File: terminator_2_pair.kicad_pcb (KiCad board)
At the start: 2 copper layers, 70.5 x 41.9 mm, 1 part

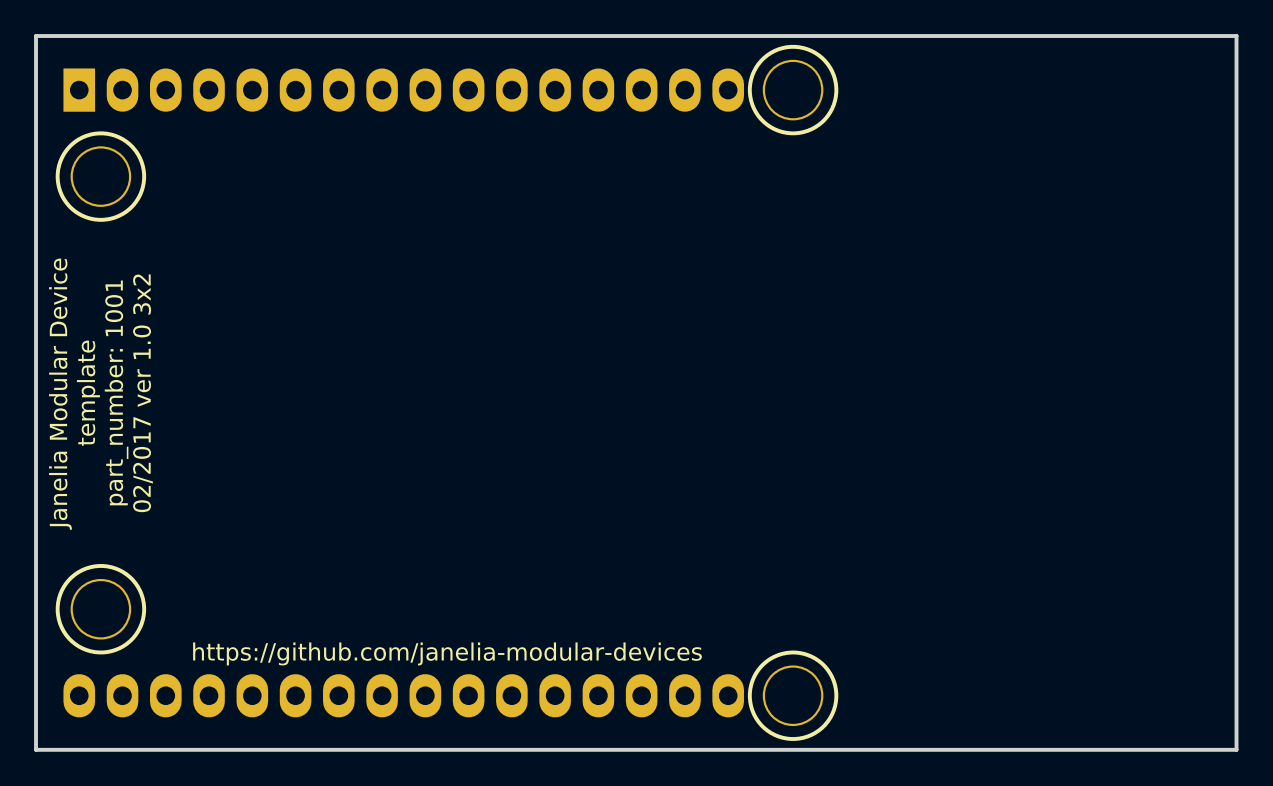
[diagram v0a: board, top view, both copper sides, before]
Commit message: Added footprints and components.
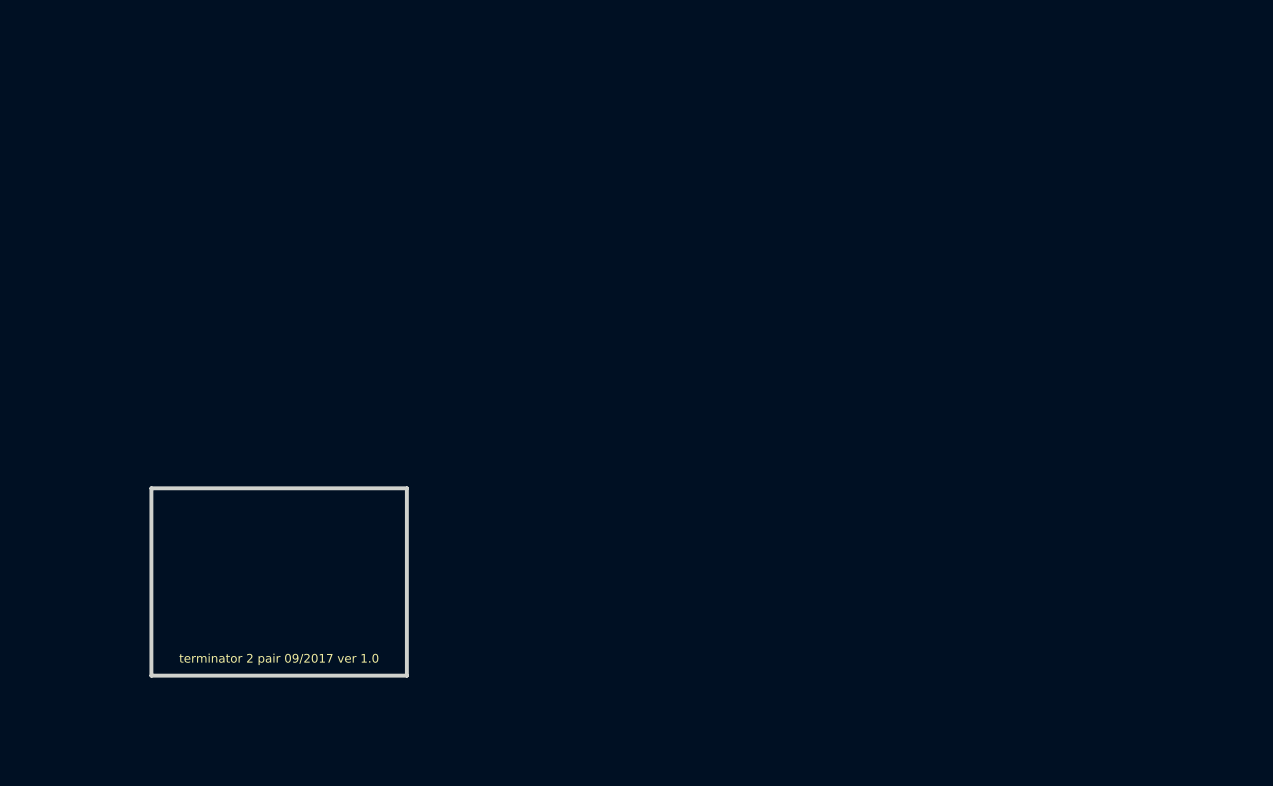
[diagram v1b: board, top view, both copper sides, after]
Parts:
- removed MDB1: MODULAR_DEVICE_BASE_3X2_MALE, terminator_2_pair:MODULAR_DEVICE_BASE_3X2_MALE
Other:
- board size 70.5 x 41.9 mm -> 15 x 11 mm
- net class Default: trace_width 0.254 -> 0.25
- board text added: "terminator 2 pair 09/2017 ver 1.0"
- board text removed: "Janelia Modular Device template part_number: 1001 02/2017 ver 1.0 3x2"
- board text removed: "https://github.com/janelia-modular-devices"
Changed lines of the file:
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@@
-(kicad_pcb (version 20170123) (host pcbnew no-vcs-found-0633d90~59~ubuntu16.04.1)
+(kicad_pcb (version 20170123) (host pcbnew no-vcs-found-33cc7b3~60~ubuntu16.04.1)
   (general
     (thickness 1.6)
-    (drawings 6)
+    (drawings 5)
     (tracks 0)
     (zones 0)
-    (modules 1)
+    (modules 0)
     (nets 1)
   )
@@
   )
   (setup
-    (last_trace_width 0.254)
+    (last_trace_width 0.25)
     (trace_clearance 0.0254)
     (zone_clearance 0.2032)
@@
       (layerselection 0x000f0_ffffffff)
       (usegerberextensions true)
+      (usegerberattributes true)
+      (usegerberadvancedattributes true)
+      (creategerberjobfile true)
       (excludeedgelayer false)
       (linewidth 0.100000)
@@
   (net_class Default "This is the default net class."
     (clearance 0.0254)
-    (trace_width 0.254)
+    (trace_width 0.25)
     (via_dia 0.889)
     (via_drill 0.635)
     (uvia_dia 0.508)
     (uvia_drill 0.127)
-    (diff_pair_gap 0.254)
-    (diff_pair_width 0.254)
   )
   (net_class GND ""
@@
     (diff_pair_width 0.254)
   )
-  (module terminator_2_pair:MODULAR_DEVICE_BASE_3X2_MALE (layer F.Cu)
-    (at 107.315 88.9)
-    (fp_text reference MDB1 (at 0 0) (layer F.SilkS) hide
-      (effects (font (size 1.016 1.016) (thickness 0.254)))
-    )
-    (fp_text value MODULAR_DEVICE_BASE_3X2_MALE (at 0 2.54) (layer F.SilkS) hide
-      (effects (font (thickness 0.3048)))
-    )
-    (fp_line (start 48.895 -20.955) (end -21.59 -20.955) (layer F.Fab) (width 0.2286))
-    (fp_line (start 48.895 20.955) (end 48.895 -20.955) (layer F.Fab) (width 0.2286))
-    (fp_line (start -21.59 20.955) (end 48.895 20.955) (layer F.Fab) (width 0.2286))
-    (fp_line (start -21.59 -20.955) (end -21.59 20.955) (layer F.Fab) (width 0.2286))
-    (fp_line (start 20.32 -19.05) (end -20.32 -19.05) (layer B.SilkS) (width 0.381))
-    (fp_line (start 20.32 -16.51) (end 20.32 -19.05) (layer B.SilkS) (width 0.381))
-    (fp_line (start -20.32 -16.51) (end 20.32 -16.51) (layer B.SilkS) (width 0.381))
-    (fp_line (start -20.32 -19.05) (end -20.32 -16.51) (layer B.SilkS) (width 0.381))
-    (fp_line (start 20.32 16.51) (end -20.32 16.51) (layer B.SilkS) (width 0.381))
-    (fp_line (start 20.32 19.05) (end 20.32 16.51) (layer B.SilkS) (width 0.381))
-    (fp_line (start -20.32 19.05) (end 20.32 19.05) (layer B.SilkS) (width 0.381))
-    (fp_line (start -20.32 16.51) (end -20.32 19.05) (layer B.SilkS) (width 0.381))
-    (fp_circle (center 22.86 -17.78) (end 25.4 -17.78) (layer F.SilkS) (width 0.2286))
-    (fp_circle (center 22.86 17.78) (end 25.4 17.78) (layer F.SilkS) (width 0.2286))
-    (fp_circle (center -17.78 12.7) (end -15.24 12.7) (layer F.SilkS) (width 0.2286))
-    (fp_circle (center -17.78 -12.7) (end -15.24 -12.7) (layer F.SilkS) (width 0.2286))
-    (pad "" thru_hole circle (at 22.86 -17.78) (size 3.556 3.556) (drill 3.302) (layers *.Cu *.Mask F.SilkS))
-    (pad "" thru_hole circle (at 22.86 17.78) (size 3.556 3.556) (drill 3.302) (layers *.Cu *.Mask F.SilkS))
-    (pad "" thru_hole circle (at -17.78 12.7) (size 3.556 3.556) (drill 3.302) (layers *.Cu *.Mask F.SilkS))
-    (pad "" thru_hole circle (at -17.78 -12.7) (size 3.556 3.556) (drill 3.302) (layers *.Cu *.Mask F.SilkS))
-    (pad AREF thru_hole oval (at -19.05 17.78) (size 1.8542 2.54) (drill 1.0922) (layers *.Cu *.Mask))
-    (pad VEE thru_hole oval (at -16.51 17.78) (size 1.8542 2.54) (drill 1.0922) (layers *.Cu *.Mask))
-    (pad AGND thru_hole oval (at -13.97 17.78) (size 1.8542 2.54) (drill 1.0922) (layers *.Cu *.Mask))
-    (pad 3V3 thru_hole oval (at -11.43 17.78) (size 1.8542 2.54) (drill 1.0922) (layers *.Cu *.Mask))
-    (pad 23 thru_hole oval (at -8.89 17.78) (size 1.8542 2.54) (drill 1.0922) (layers *.Cu *.Mask))
-    (pad 22 thru_hole oval (at -6.35 17.78) (size 1.8542 2.54) (drill 1.0922) (layers *.Cu *.Mask))
-    (pad 21 thru_hole oval (at -3.81 17.78) (size 1.8542 2.54) (drill 1.0922) (layers *.Cu *.Mask))
-    (pad 20 thru_hole oval (at -1.27 17.78) (size 1.8542 2.54) (drill 1.0922) (layers *.Cu *.Mask))
-    (pad 19 thru_hole oval (at 1.27 17.78) (size 1.8542 2.54) (drill 1.0922) (layers *.Cu *.Mask))
-    (pad 18 thru_hole oval (at 3.81 17.78) (size 1.8542 2.54) (drill 1.0922) (layers *.Cu *.Mask))
-    (pad 17 thru_hole oval (at 6.35 17.78) (size 1.8542 2.54) (drill 1.0922) (layers *.Cu *.Mask))
-    (pad 16 thru_hole oval (at 8.89 17.78) (size 1.8542 2.54) (drill 1.0922) (layers *.Cu *.Mask))
-    (pad 15 thru_hole oval (at 11.43 17.78) (size 1.8542 2.54) (drill 1.0922) (layers *.Cu *.Mask))
-    (pad 14 thru_hole oval (at 13.97 17.78) (size 1.8542 2.54) (drill 1.0922) (layers *.Cu *.Mask))
-    (pad 13 thru_hole oval (at 16.51 17.78) (size 1.8542 2.54) (drill 1.0922) (layers *.Cu *.Mask))
-    (pad DAC thru_hole oval (at 19.05 17.78) (size 1.8542 2.54) (drill 1.0922) (layers *.Cu *.Mask))
-    (pad 28 thru_hole oval (at 19.05 -17.78) (size 1.8542 2.54) (drill 1.0922) (layers *.Cu *.Mask))
-    (pad 12 thru_hole oval (at 16.51 -17.78) (size 1.8542 2.54) (drill 1.0922) (layers *.Cu *.Mask))
-    (pad 11 thru_hole oval (at 13.97 -17.78) (size 1.8542 2.54) (drill 1.0922) (layers *.Cu *.Mask))
-    (pad 10 thru_hole oval (at 11.43 -17.78) (size 1.8542 2.54) (drill 1.0922) (layers *.Cu *.Mask))
-    (pad 9 thru_hole oval (at 8.89 -17.78) (size 1.8542 2.54) (drill 1.0922) (layers *.Cu *.Mask))
-    (pad 29 thru_hole oval (at 6.35 -17.78) (size 1.8542 2.54) (drill 1.0922) (layers *.Cu *.Mask))
-    (pad 30 thru_hole oval (at 3.81 -17.78) (size 1.8542 2.54) (drill 1.0922) (layers *.Cu *.Mask))
-    (pad 6 thru_hole oval (at 1.27 -17.78) (size 1.8542 2.54) (drill 1.0922) (layers *.Cu *.Mask))
-    (pad 5 thru_hole oval (at -1.27 -17.78) (size 1.8542 2.54) (drill 1.0922) (layers *.Cu *.Mask))
-    (pad 4 thru_hole oval (at -3.81 -17.78) (size 1.8542 2.54) (drill 1.0922) (layers *.Cu *.Mask))
-    (pad 3 thru_hole oval (at -6.35 -17.78) (size 1.8542 2.54) (drill 1.0922) (layers *.Cu *.Mask))
-    (pad 2 thru_hole oval (at -8.89 -17.78) (size 1.8542 2.54) (drill 1.0922) (layers *.Cu *.Mask))
-    (pad 25 thru_hole oval (at -11.43 -17.78) (size 1.8542 2.54) (drill 1.0922) (layers *.Cu *.Mask))
-    (pad VDD thru_hole rect (at -19.05 -17.78) (size 1.8542 2.54) (drill 1.0922) (layers *.Cu *.Mask))
-    (pad 24 thru_hole oval (at -13.97 -17.78) (size 1.8542 2.54) (drill 1.0922) (layers *.Cu *.Mask))
-    (pad GND thru_hole oval (at -16.51 -17.78) (size 1.8542 2.54) (drill 1.0922) (layers *.Cu *.Mask))
-  )
-  (gr_line (start 156.21 67.945) (end 85.725 67.945) (angle 90) (layer Edge.Cuts) (width 0.2286))
-  (gr_line (start 156.21 109.855) (end 156.21 67.945) (angle 90) (layer Edge.Cuts) (width 0.2286))
-  (gr_line (start 85.725 109.855) (end 156.21 109.855) (angle 90) (layer Edge.Cuts) (width 0.2286))
-  (gr_line (start 85.725 67.945) (end 85.725 109.855) (angle 90) (layer Edge.Cuts) (width 0.2286))
-  (gr_text https://github.com/janelia-modular-devices (at 109.855 104.14) (layer F.SilkS)
-    (effects (font (size 1.016 1.016) (thickness 0.1905)))
-  )
-  (gr_text "Janelia Modular Device\ntemplate\npart_number: 1001\n02/2017 ver 1.0 3x2" (at 89.535 88.9 90) (layer F.SilkS)
-    (effects (font (size 1.016 1.016) (thickness 0.254)))
+  (gr_line (start 107.5 94.5) (end 92.5 94.5) (angle 90) (layer Edge.Cuts) (width 0.2286))
+  (gr_line (start 107.5 105.5) (end 107.5 94.5) (angle 90) (layer Edge.Cuts) (width 0.2286))
+  (gr_line (start 92.5 105.5) (end 107.5 105.5) (angle 90) (layer Edge.Cuts) (width 0.2286))
+  (gr_line (start 92.5 94.5) (end 92.5 105.5) (angle 90) (layer Edge.Cuts) (width 0.2286))
+  (gr_text "terminator 2 pair 09/2017 ver 1.0" (at 100 104.5) (layer F.SilkS)
+    (effects (font (size 0.508 0.508) (thickness 0.127)))
   )
 )
